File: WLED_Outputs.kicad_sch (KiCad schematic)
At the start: 58 parts, among them Q901 NTLJS17D0P03P8Z, U901 74LV1T125, U902 74LV1T125, U903 TPS2HCS10A-Q1, U904 74LV1T125, U905 74LV1T125, U906 74LV1T125, U907 74LV1T125

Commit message: Update .gitignore, CANBus_Interface.kicad_sch, ESP32-S3_WLED_UnderGlow_Hat-2026-05-04_233126.zip, and 17 more files
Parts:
- removed C906, C916: 0.1uF, My Capacitors:C_0201_Dense, symbol Device:C_Small
- added C906, C916: 0.1uF, My Capacitors:C_0201_Dense, symbol Device:C
- C901, C902, C903, C904, C905, C907, C908, C909, C910, C911, C912, C913, C914, C915: symbol Device:C_Small -> Device:C
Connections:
- net SDO_{HSS} is gone; now on net SDO: R906.1, U903.14 (SDO)
- net +3V3: now also R901.1; no longer R901.2
- net +V_{SW}: now also C916.1
- net GND: now also C916.2
- net RLY-: now also C906.2
- net SDO: no longer R906.2
- net VDD_{HSS}: now also R901.2; no longer R901.1
- net V_{OUT1}: now also C906.1
- new net MISO: R906.2
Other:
- moved on the sheet: D901, D904, D912, R901, R914

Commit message: replaced Device:C with Device:C_Small and Device:R with Device:R_Small
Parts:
- C901, C902, C903, C904, C905, C906, C907, C908, C909, C910, C911, C912, C913, C914, C915, C916: symbol Device:C -> Device:C_Small
- R901, R902, R903, R904, R905, R906, R907, R908, R909, R910, R911, R912, R913, R914, R915, R916, R917, R918: symbol Device:R -> Device:R_Small
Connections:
- net SDO renamed SDO_{HSS}

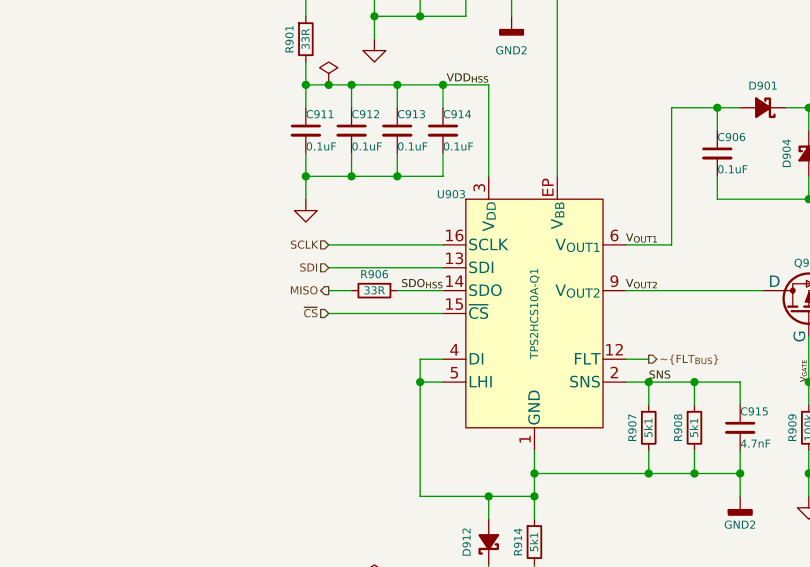
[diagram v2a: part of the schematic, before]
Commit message: Updated Net Names for FSPI and I2S nets
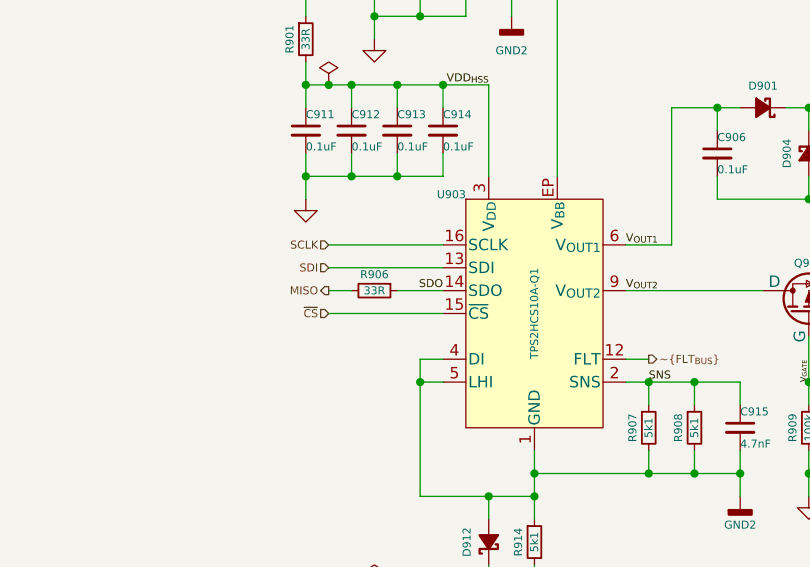
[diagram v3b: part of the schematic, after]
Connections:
- net SDO_{HSS} renamed SDO
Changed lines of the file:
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@@
 		)
 	)
-	(label "SDO_{HSS}"
+	(label "SDO"
 		(at 203.2 91.44 180)
 		(effects

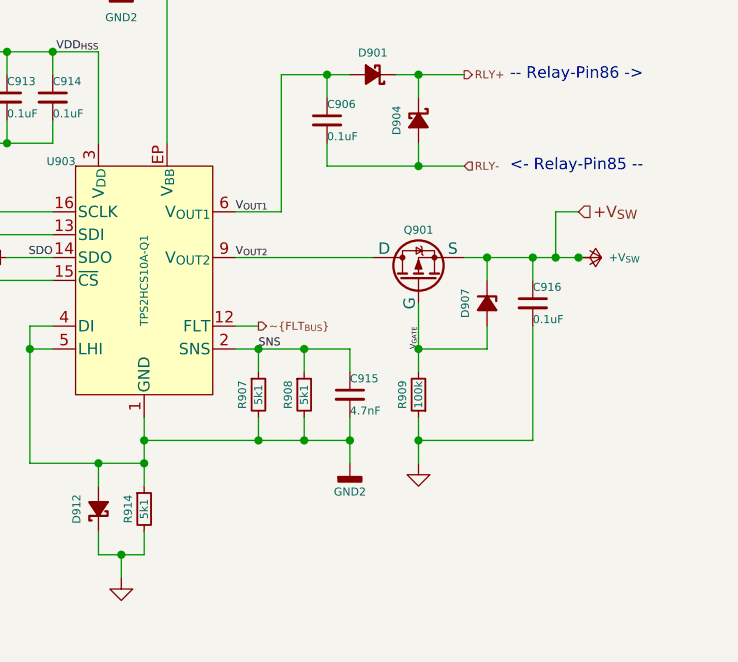
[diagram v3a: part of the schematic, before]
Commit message: schematic updated with new ESP32-S3_D1_Pico symbol
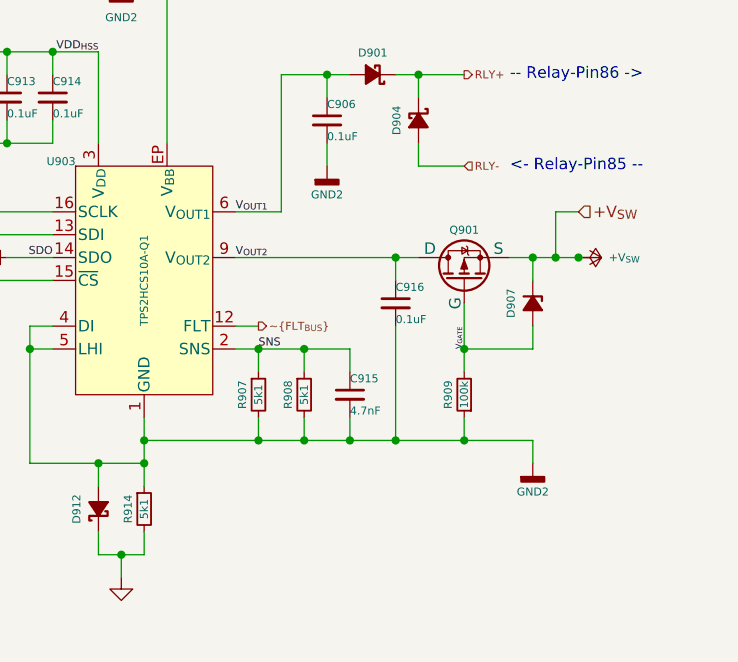
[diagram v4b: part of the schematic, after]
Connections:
- net +V_{SW}: no longer C916.1
- net GND: no longer C916.2, R909.1
- net GND2: now also C906.2, C916.2, R909.1
- net RLY-: no longer C906.2
- net V_{OUT2}: now also C916.1
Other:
- moved on the sheet: C916, D907, Q901, R909

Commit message: JLCPCB: W2026061412450502 2026-06-14 PCB: Y62-5297522A PCBA: SMT026061460215-5297522A
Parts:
- D901, D902, D903, D904, D908, D909, D912, D913, D914: footprint Personal_FootprintLibrary:DSN0603-2 -> My Package_Leadless:DFN0603-2
